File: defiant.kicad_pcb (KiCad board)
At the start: 2 copper layers, 126.4 x 98 mm, 48 parts, among them J1 Conn_01x02_Pin, T0 SW_PUSH, T1 SW_PUSH, T2 SW_PUSH, T3 SW_PUSH, T4 SW_PUSH, U1 Seeed Studio XIAO BLE

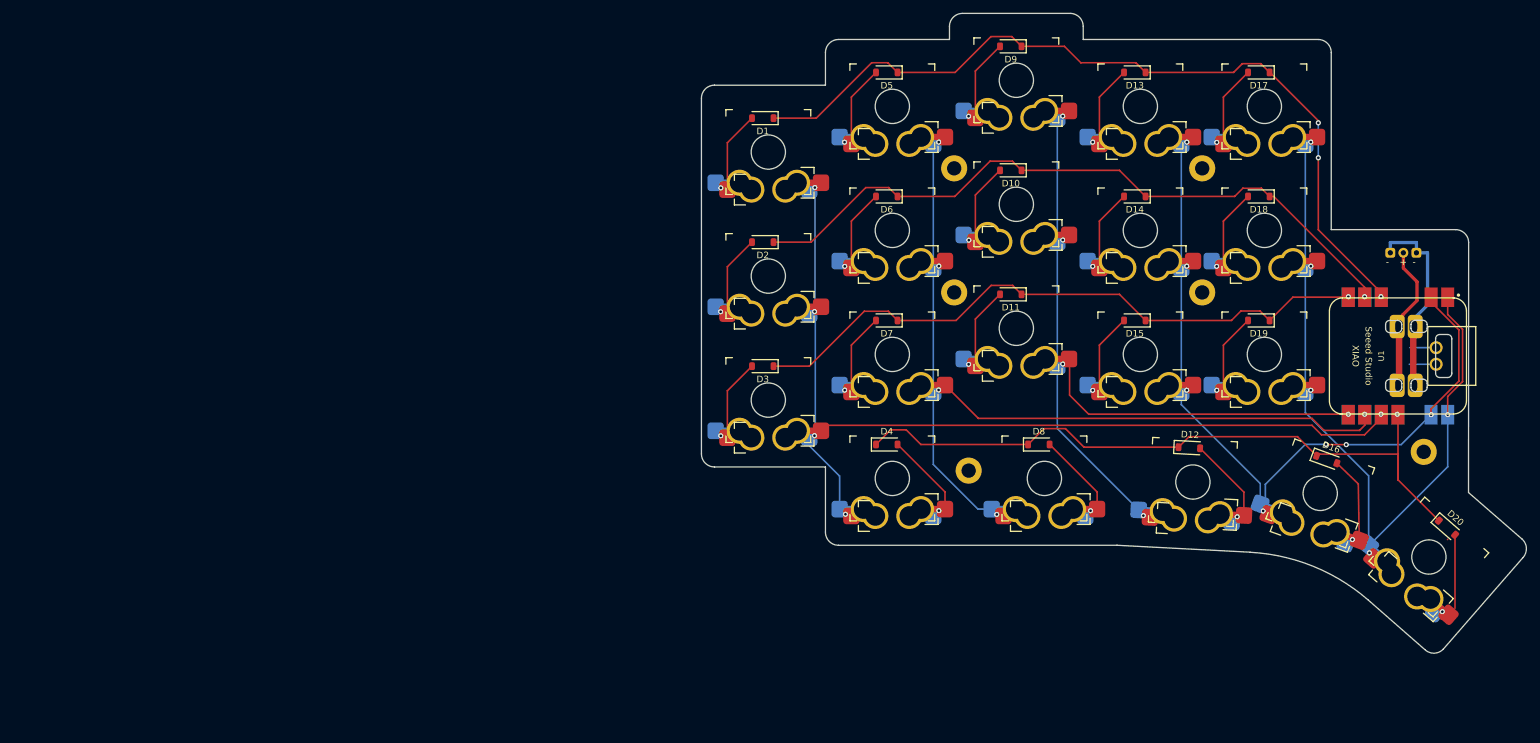
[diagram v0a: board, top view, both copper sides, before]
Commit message: Change thumb pad to regular keys
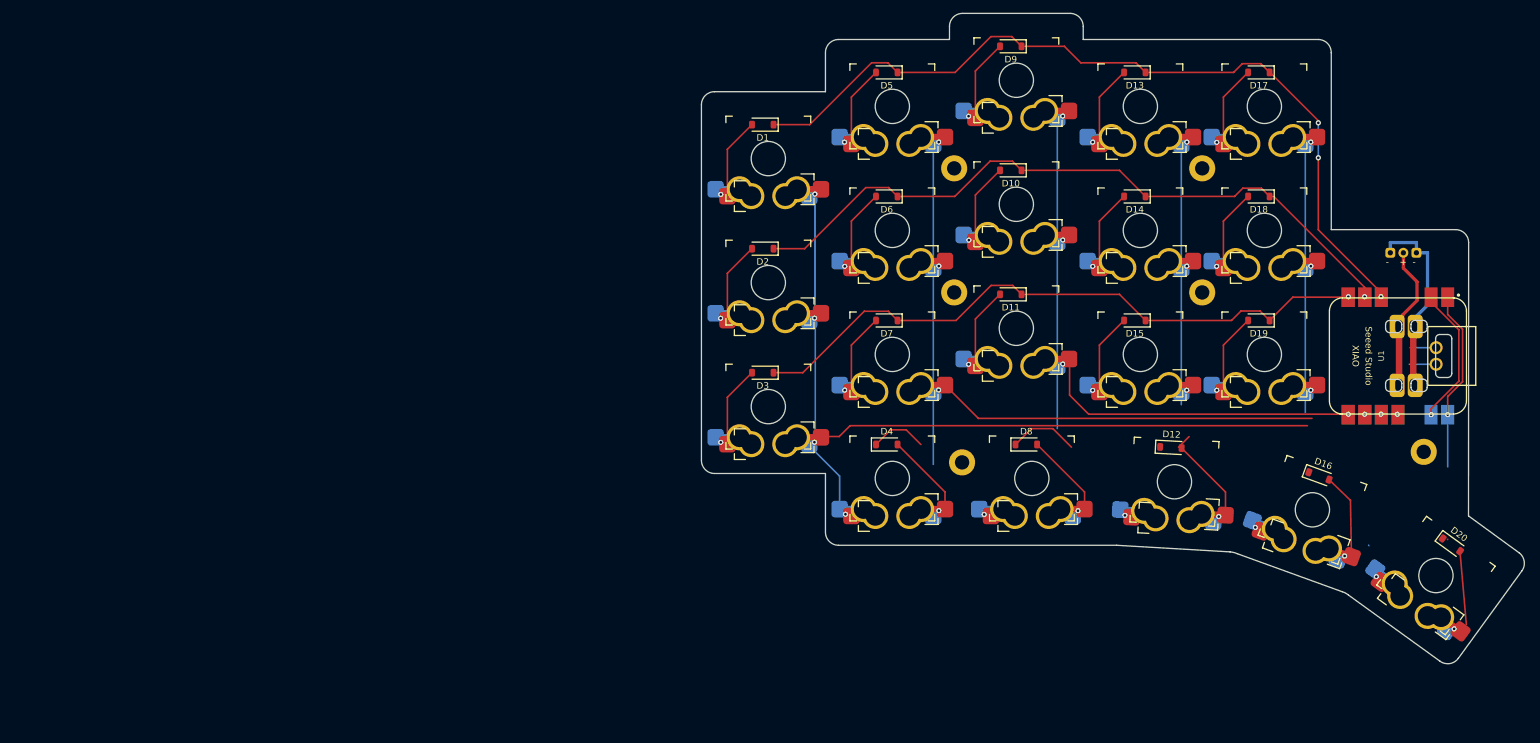
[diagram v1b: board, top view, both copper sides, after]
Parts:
- moved T4 3.04 mm to (297.7, 123.8), turned to -36 degrees
- moved D12 2.82 mm to (257.1, 104.2)
- moved T2 2.82 mm to (257.7, 109.4)
- moved T3 2.79 mm to (278.8, 113.7)
- moved D16 2.79 mm to (279.8, 108.5)
- moved D20 2.71 mm to (300.1, 119.1), turned to -36 degrees
- moved D8 1.93 mm to (235.0, 103.7)
- moved T1 1.93 mm to (235.8, 108.9)
- moved ? 1.61 mm to (225.1, 106.5)
- moved C0R1 1.00 mm to (195.4, 59.9)
- moved C0R2 1.00 mm to (195.4, 78.9)
- moved C0R3 1.00 mm to (195.4, 97.9)
- moved D1 1.00 mm to (194.6, 54.7)
- moved D2 1.00 mm to (194.6, 73.7)
- moved D3 1.00 mm to (194.6, 92.7)
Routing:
- net row3: track 108.8 -> 19.5 mm
- net col3: track 114.9 -> 61.5 mm, vias 7 -> 5
- net col4: track 110.5 -> 69.1 mm
- net col1: track 130.0 -> 107.4 mm
- net col2: track 114.7 -> 97.1 mm
- net col0: track 139.5 -> 128.1 mm
- net Net-(D12-A): track 13.1 -> 15.3 mm
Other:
- board size 126.4 x 98 mm -> 126.1 x 99.6 mm

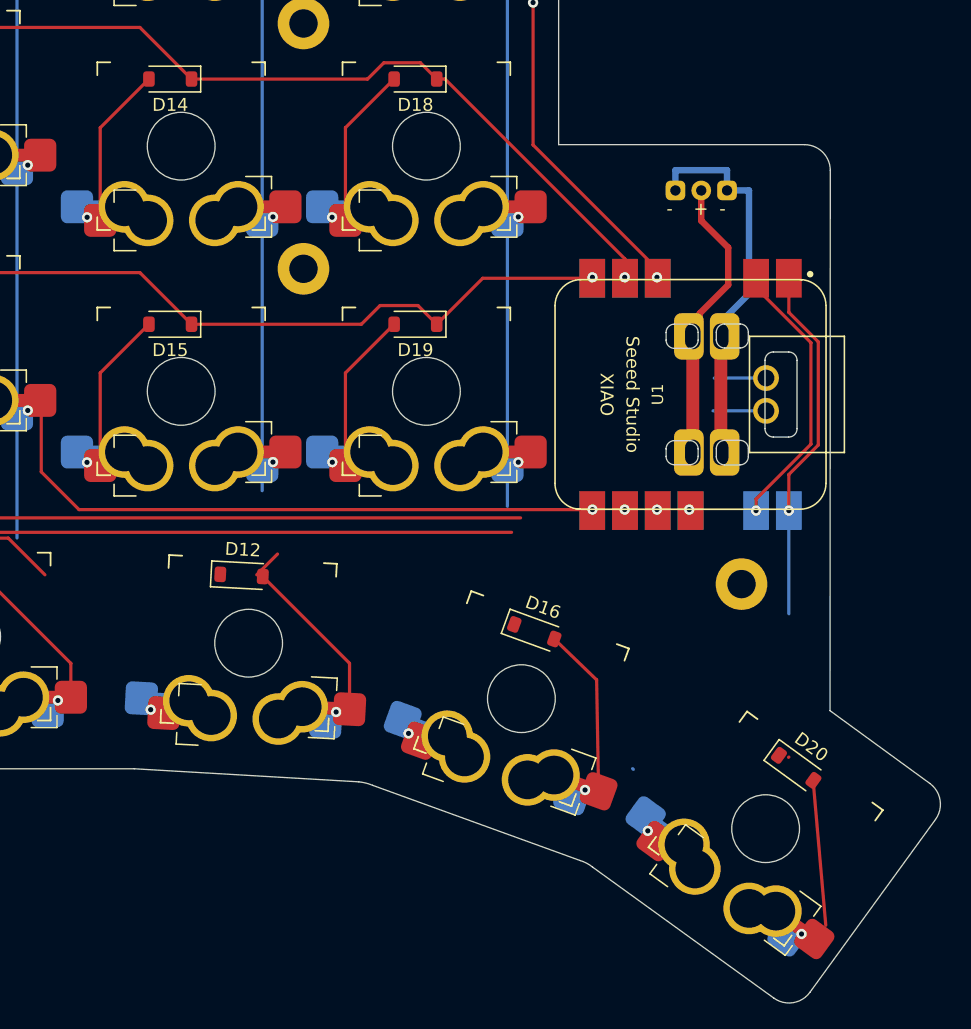
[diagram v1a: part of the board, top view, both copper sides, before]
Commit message: Move home thumb key up
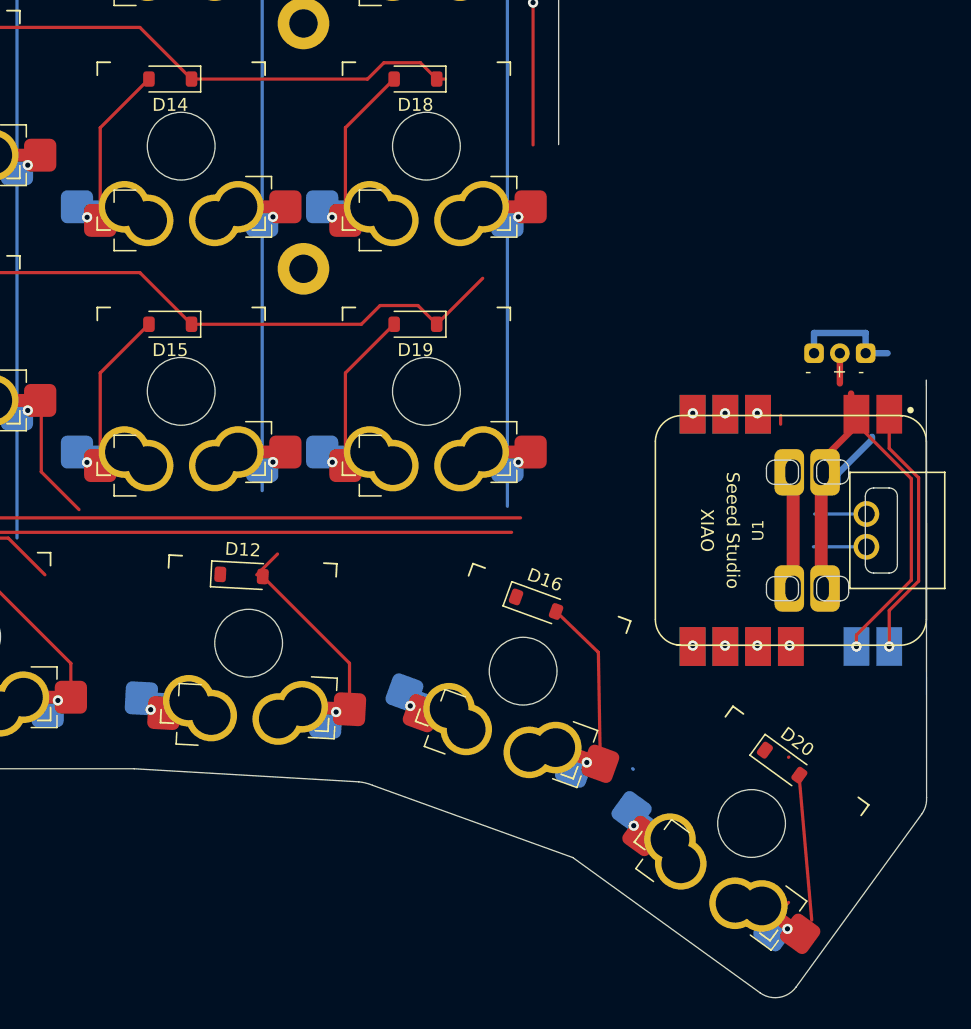
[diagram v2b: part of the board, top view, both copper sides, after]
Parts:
- removed the ? at (295.9, 104.8)
- moved J1 16.6 mm to (303.5, 87.0)
- moved U1 13.1 mm to (299.7, 100.7)
- moved D16 2.13 mm to (279.9, 106.4)
- moved T3 2.13 mm to (278.9, 111.6)
- moved T4 1.16 mm to (296.6, 123.4)
- moved D20 1.16 mm to (299.0, 118.7)
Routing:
- net col2: track 97.1 -> 57.3 mm
- net row1: track 107.8 -> 86.6 mm
- net row0: track 127.8 -> 115.6 mm
- net row2: track 99.7 -> 91.2 mm
- net col4: track 69.1 -> 61.1 mm
- net Net-(J1-Pin_1): track 30.3 -> 22.5 mm
- net Net-(J1-Pin_2): track 22.1 -> 19.1 mm
- net row3: track 19.5 -> 20.0 mm
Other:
- board size 126.1 x 99.6 mm -> 125 x 99.2 mm

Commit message: Update footprints
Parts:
- added C5R2: SW_PUSH, Defiant:SW_Gateron_LowProfile_HotSwap_PTH_Reversible, F.Cu at (185.0, 71.4)
- added C5R3: SW_PUSH, Defiant:SW_Gateron_LowProfile_HotSwap_PTH_Reversible, F.Cu at (185.0, 90.4)
- added D22: D, Diode_SMD:D_SOD-123, F.Cu at (184.2, 66.3)
- added D23: D, Diode_SMD:D_SOD-123, F.Cu at (184.2, 85.3)
- moved D16 106.2 mm to (174.4, 118.7)
- moved T3 106.2 mm to (173.4, 123.9)
- moved C4R1 105.9 mm to (166.0, 62.1)
- moved C4R2 105.9 mm to (166.0, 81.1)
- moved C4R3 105.9 mm to (166.0, 100.1)
- moved REF** 105.9 mm to (156.5, 71.6)
- moved REF** 105.9 mm to (156.5, 90.6)
- moved T2 105.9 mm to (152.2, 119.6)
- moved ? 105.9 mm to (119.7, 116.6)
- moved C2R1 105.9 mm to (128.0, 58.1)
- moved C2R2 105.9 mm to (128.0, 77.1)
- moved C2R3 105.9 mm to (128.0, 96.1)
- moved C3R1 105.9 mm to (147.0, 62.1)
- moved C3R2 105.9 mm to (147.0, 81.1)
- moved C3R3 105.9 mm to (147.0, 100.1)
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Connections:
- U1 pad 19: unconnected-(U1-RESET-Pad19) -> Net-(U1-RESET)
- U1 pad 20: unconnected-(U1-GND-Pad20) -> Net-(SW1-Pad2)
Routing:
- net row3: track 20.0 -> 107.0 mm
- net col3: track 61.5 -> 130.3 mm
- net col4: track 61.1 -> 116.4 mm
- net row1: track 86.6 -> 107.2 mm
- net col5: track 0.00 -> 19.0 mm
- net row0: track 115.6 -> 96.7 mm, vias 3 -> 1
- net col2: track 57.3 -> 73.7 mm
- net Net-(D22-A): track 0.00 -> 16.0 mm
- net Net-(D23-A): track 0.00 -> 15.9 mm
- net row2: track 91.2 -> 105.9 mm
- net col0: track 127.6 -> 141.1 mm
- net col1: track 107.4 -> 118.0 mm
- net Net-(J1-Pin_2): track 19.1 -> 11.3 mm
- net Net-(SW1-Pad2): track 0.00 -> 4.10 mm
- net unconnected-(U1-GND-Pad20): track 4.10 -> 0.00 mm
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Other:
- board size 125 x 99.2 mm -> 126.6 x 99.6 mm

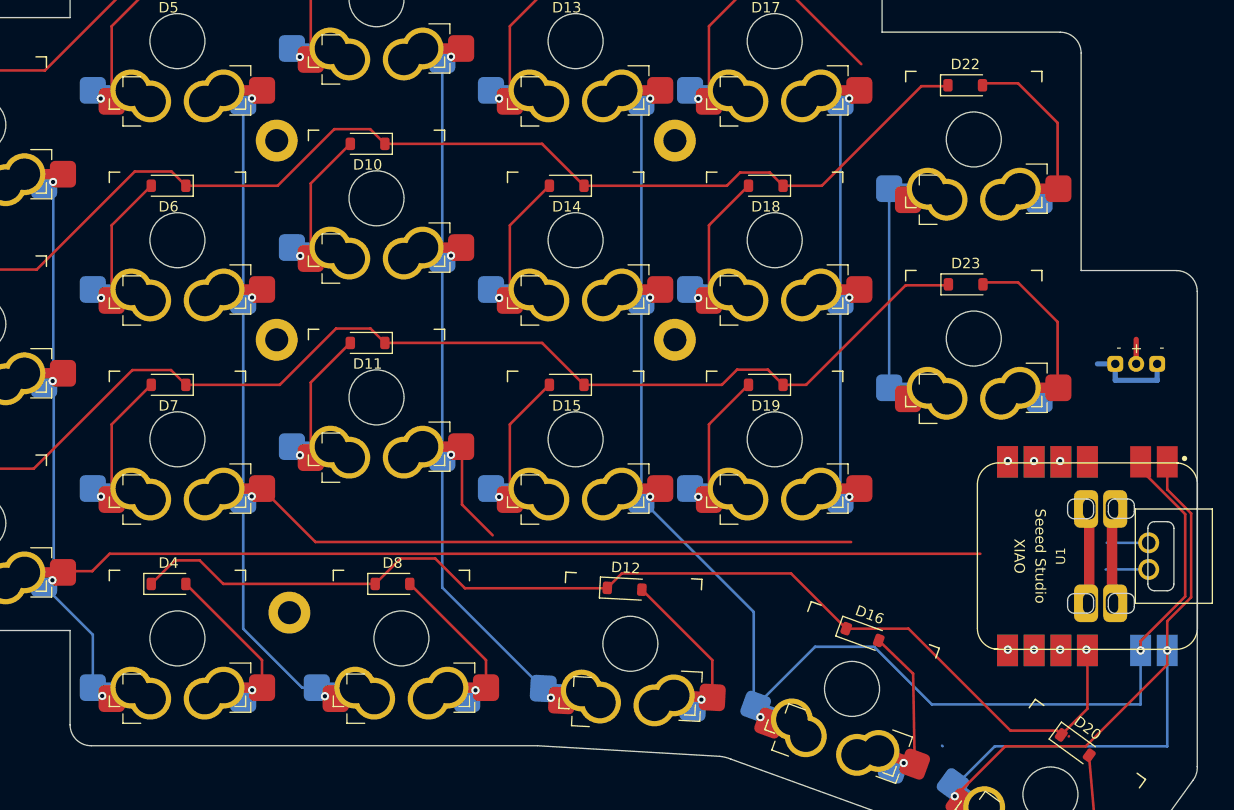
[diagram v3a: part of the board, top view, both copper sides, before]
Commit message: Add power switch and reset button
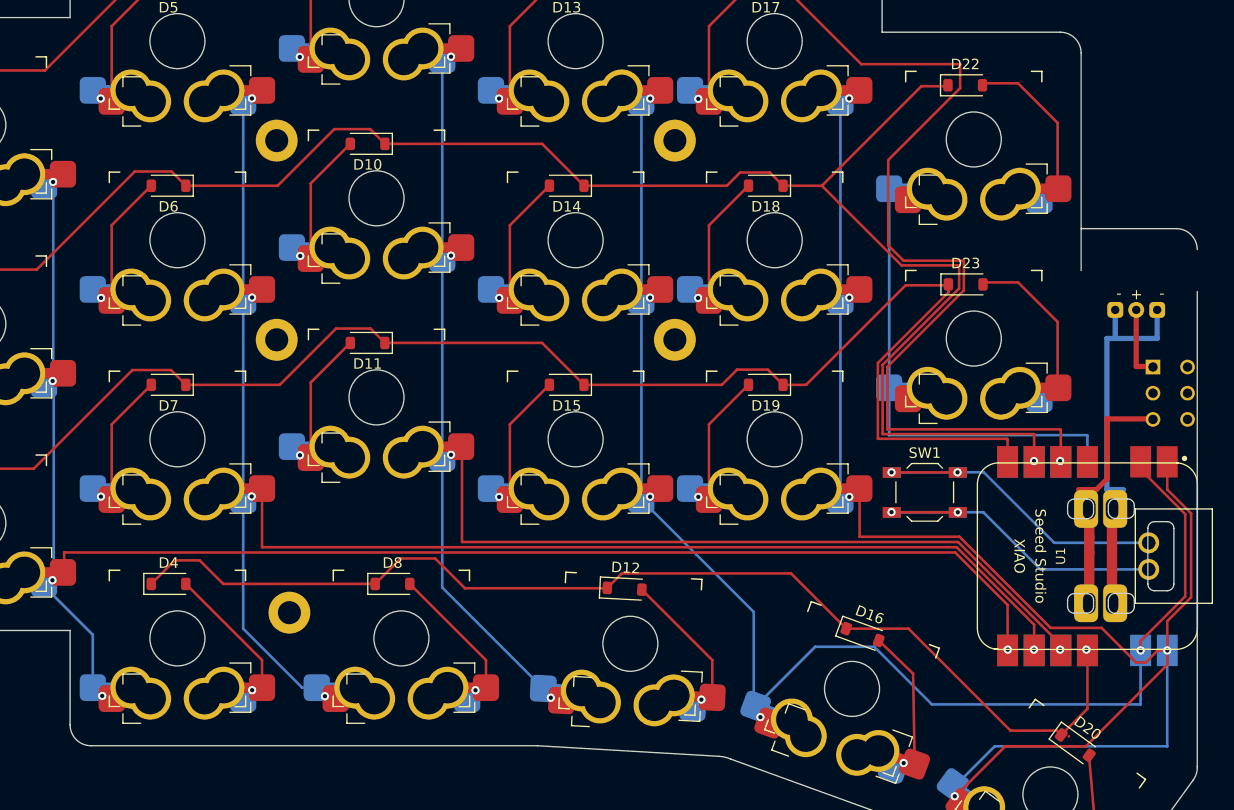
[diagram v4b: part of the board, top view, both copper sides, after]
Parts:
- added SW1: SW_Push, Button_Switch_SMD:SW_SPST_TL3342, F.Cu at (180.3, 105.1)
- added SW2: SW_Push, Button_Switch_SMD:SW_SPST_TL3342, B.Cu at (180.3, 105.1)
- added SW3: SW_DP3T, Button_Switch_THT:SW_CuK_JS202011AQN_DPDT_Angled, B.Cu at (202.1, 93.2)
- moved J1 5.15 mm to (200.5, 87.7)
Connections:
- U1 pad 10: col0 -> col2
- U1 pad 22: Net-(J1-Pin_2) -> Net-(U1-BAT+)
- U1 pad 4: (no net) -> col5
- U1 pad 8: col2 -> col0
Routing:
- net row0: track 96.7 -> 172.9 mm
- net col2: track 73.7 -> 135.4 mm
- net row1: track 107.2 -> 159.6 mm
- net col4: track 116.4 -> 155.7 mm
- net row2: track 105.9 -> 138.0 mm, vias 1 -> 0
- net Net-(U1-RESET): track 4.00 -> 33.6 mm, vias 0 -> 2
- net Net-(SW1-Pad2): track 4.10 -> 33.1 mm, vias 0 -> 2
- net col1: track 118.0 -> 144.5 mm
- net col5: track 19.0 -> 45.0 mm
- net Net-(U1-BAT+): track 0.00 -> 23.0 mm
- net Net-(J1-Pin_1): track 18.5 -> 36.5 mm
- net col0: track 141.1 -> 150.7 mm
- net Net-(J1-Pin_2): track 11.3 -> 7.06 mm
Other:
- outline, holes or cut-outs redrawn

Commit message: Create JLCPCB production files
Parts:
- added ?: , , F.Cu at (181.2, 113.7)
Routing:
- net Net-(D20-A): track 12.6 -> 11.2 mm
- net col0: track 150.7 -> 149.5 mm
- net col2: track 135.4 -> 134.9 mm
- net row2: track 138.0 -> 137.9 mm, vias 0 -> 1
- net col5: vias 0 -> 3
- net Net-(D23-A): vias 0 -> 1
- net Net-(D22-A): vias 0 -> 1
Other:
- outline, holes or cut-outs redrawn
- board text added: "Defiant v0.1"
- board text added: "JLCJLCJLCJLC"
- board text added: "Mik Müller Special Edition"
- board text added: "by Antonius Naumann"
